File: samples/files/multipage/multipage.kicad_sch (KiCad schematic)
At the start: 1 part

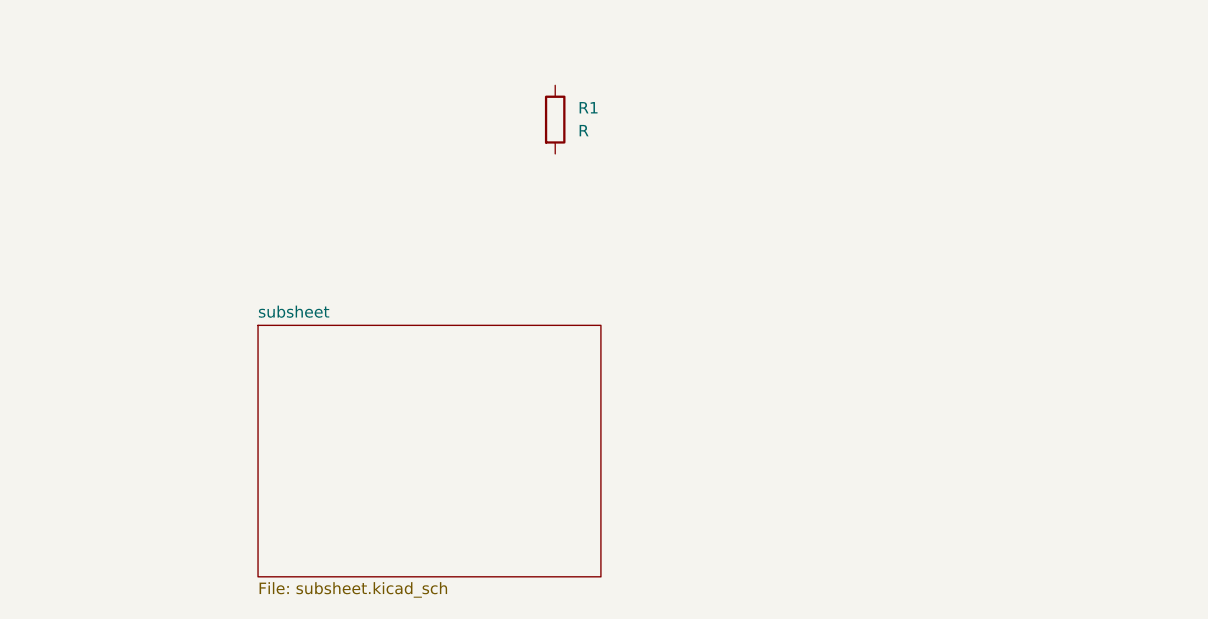
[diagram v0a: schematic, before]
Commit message: implement all schema elements
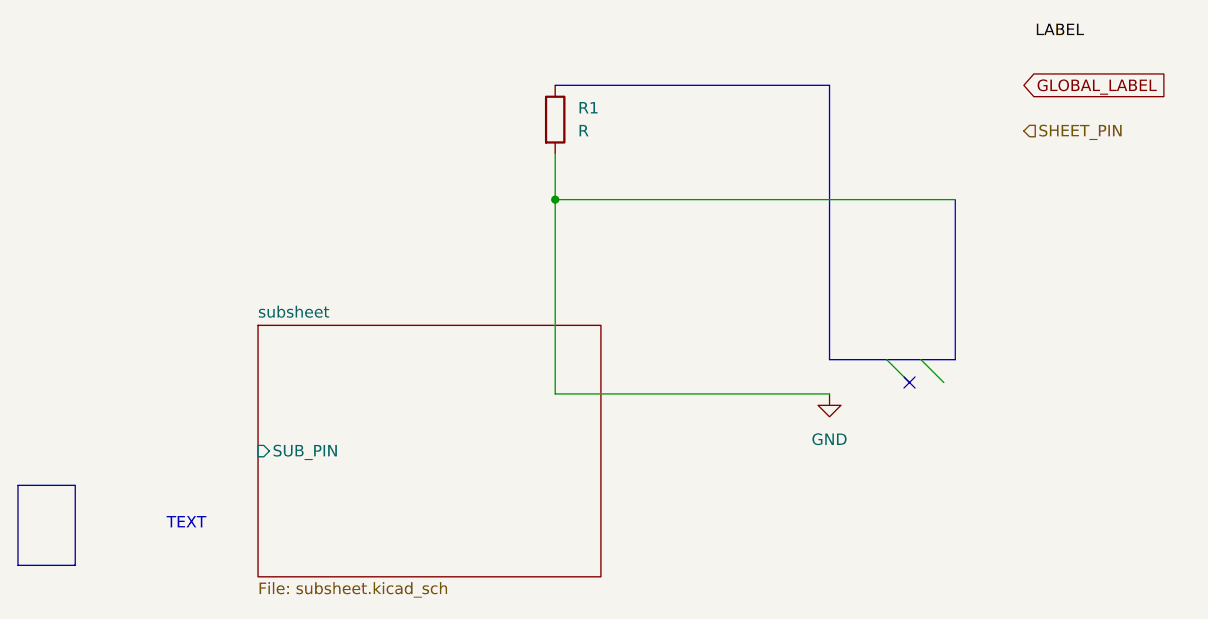
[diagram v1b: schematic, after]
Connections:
- net GND: now reaches R1.2
- no-connect marks 0 -> 1
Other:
- sheet subsheet ports: added SUB_PIN; removed none
- note added: "TEXT"
- company: (none) -> private
- title: (none) -> Schema with all elements
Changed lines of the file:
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@@
 (kicad_sch (version 20211123) (generator eeschema)
   (paper "A4")
+  (title_block
+    (title "Schema with all elements")
+    (date "2022-09-05")
+    (rev "R01")
+    (company "private")
+  )
+  (junction (at 148.59 69.85) (diameter 0) (color 0 0 0 0)
+  )
+  (no_connect (at 187.96 90.17))
+  (bus_entry (at 189.23 87.63) (size 2.54 2.54)
+    (stroke (width 0) (type default) (color 0 0 0 0))
+  )
+  (bus_entry (at 185.42 87.63) (size 2.54 2.54)
+    (stroke (width 0) (type default) (color 0 0 0 0))
+  )
+  (bus (pts (xy 189.23 87.63) (xy 193.04 87.63))
+    (stroke (width 0) (type default) (color 0 0 0 0))
+  )
+  (wire (pts (xy 148.59 69.85) (xy 148.59 91.44))
+    (stroke (width 0) (type default) (color 0 0 0 0))
+  )
+  (wire (pts (xy 179.07 91.44) (xy 148.59 91.44))
+    (stroke (width 0) (type default) (color 0 0 0 0))
+  )
+  (wire (pts (xy 148.59 69.85) (xy 193.04 69.85))
+    (stroke (width 0) (type default) (color 0 0 0 0))
+  )
+  (polyline (pts (xy 88.9 110.49) (xy 88.9 101.6))
+    (stroke (width 0) (type default) (color 0 0 0 0))
+  )
+  (bus (pts (xy 185.42 87.63) (xy 189.23 87.63))
+    (stroke (width 0) (type default) (color 0 0 0 0))
+  )
+  (bus (pts (xy 148.59 57.15) (xy 179.07 57.15))
+    (stroke (width 0) (type default) (color 0 0 0 0))
+  )
+  (bus (pts (xy 179.07 87.63) (xy 185.42 87.63))
+    (stroke (width 0) (type default) (color 0 0 0 0))
+  )
+  (wire (pts (xy 148.59 64.77) (xy 148.59 69.85))
+    (stroke (width 0) (type default) (color 0 0 0 0))
+  )
+  (polyline (pts (xy 88.9 101.6) (xy 95.25 101.6))
+    (stroke (width 0) (type default) (color 0 0 0 0))
+  )
+  (polyline (pts (xy 95.25 110.49) (xy 88.9 110.49))
+    (stroke (width 0) (type default) (color 0 0 0 0))
+  )
+  (bus (pts (xy 193.04 69.85) (xy 193.04 87.63))
+    (stroke (width 0) (type default) (color 0 0 0 0))
+  )
+  (bus (pts (xy 179.07 57.15) (xy 179.07 87.63))
+    (stroke (width 0) (type default) (color 0 0 0 0))
+  )
+  (polyline (pts (xy 95.25 101.6) (xy 95.25 110.49))
+    (stroke (width 0) (type default) (color 0 0 0 0))
+  )
+  (text "TEXT" (at 105.41 106.68 0)
+    (effects (font (size 1.27 1.27)) (justify left bottom))
+  )
+  (label "LABEL" (at 201.93 52.07 0)
+    (effects (font (size 1.27 1.27)) (justify left bottom))
+  )
+  (global_label "GLOBAL_LABEL" (shape input) (at 200.66 57.15 0) (fields_autoplaced)
+    (effects (font (size 1.27 1.27)) (justify left))
+    (property "Intersheet References" "${INTERSHEET_REFS}" (id 0) (at 216.6198 57.0706 0)
+      (effects (font (size 1.27 1.27)) (justify left) hide)
+    )
+  )
+  (hierarchical_label "SHEET_PIN" (shape input) (at 200.66 62.23 0)
+    (effects (font (size 1.27 1.27)) (justify left))
+  )
   (symbol (lib_id "Device:R") (at 148.59 60.96 0) (unit 1)
     (in_bom yes) (on_board yes) (fields_autoplaced)
@@
     (pin "2")
   )
+  (symbol (lib_id "power:GND") (at 179.07 91.44 0) (unit 1)
+    (in_bom yes) (on_board yes) (fields_autoplaced)
+    (property "Reference" "#PWR?" (id 0) (at 179.07 97.79 0)
+      (effects (font (size 1.27 1.27)) hide)
+    )
+    (property "Value" "GND" (id 1) (at 179.07 96.52 0))
+    (property "Footprint" "" (id 2) (at 179.07 91.44 0)
+      (effects (font (size 1.27 1.27)) hide)
+    )
+    (property "Datasheet" "" (id 3) (at 179.07 91.44 0)
+      (effects (font (size 1.27 1.27)) hide)
+    )
+    (pin "1")
+  )
   (sheet (at 115.57 83.82) (size 38.1 27.94) (fields_autoplaced)
     (stroke (width 0.1524) (type solid) (color 0 0 0 0))
-    (fill (color 0 0 0 0.0000))
+    (fill (color 0 0 0 0))
     (property "Sheet name" "subsheet" (id 0) (at 115.57 83.1084 0)
       (effects (font (size 1.27 1.27)) (justify left bottom))
@@
     (property "Sheet file" "subsheet.kicad_sch" (id 1) (at 115.57 112.3446 0)
       (effects (font (size 1.27 1.27)) (justify left top))
+    )
+    (pin "SUB_PIN" input (at 115.57 97.79 180)
+      (effects (font (size 1.27 1.27)) (justify left))
     )
   )
@@
   )
   (symbol_instances
+    (path "/ed83a5b9-b70a-4999-ae90-141e828bf941"
+      (reference "#PWR?") (unit 1) (value "GND") (footprint "")
+    )
     (path "/3f437e95-f712-4db4-bc87-b96fa2253386"
       (reference "R1") (unit 1) (value "R") (footprint "")
